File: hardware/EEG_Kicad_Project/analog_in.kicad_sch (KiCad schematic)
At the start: 1 part, among them U3 ADS1299

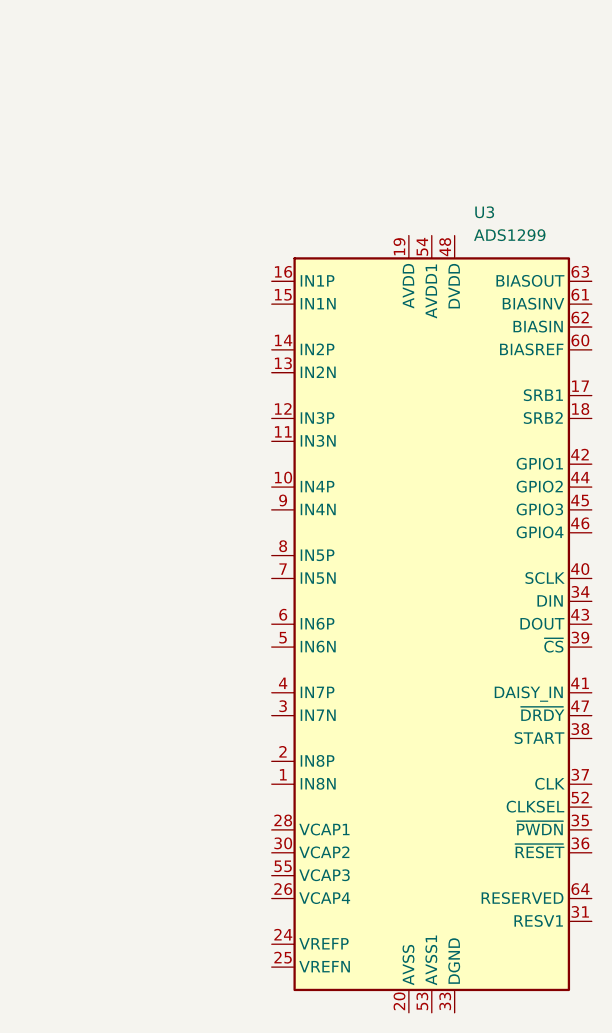
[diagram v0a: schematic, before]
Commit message: Add USB galvanic isolation barrier for patient safety
Adds a USB-C receptacle -> ESD protection -> ADuM3160 isolator ->
isolated TMU3-0511 DC-DC chain, separating the STM32/ADS1299/analog
supply (now fully isolated) from the non-isolated USB-connector side.
Closes the previously-floating USB_OTG_FS_DP/DM pins on the STM32,
adds CC1/CC2 pulldowns and VBUS decoupling on the new receptacle, and
fixes ADuM3160 VBUS2 tie per datasheet. Verified via kicad-happy: no
ERC regressions, isolation barrier confirmed intact (no net bridges
GND_PRI/+5V_PRI with the isolated GNDA/+5V/+3V3 domain).

Co-Authored-By: Claude Sonnet 5 <noreply@anthropic.com>
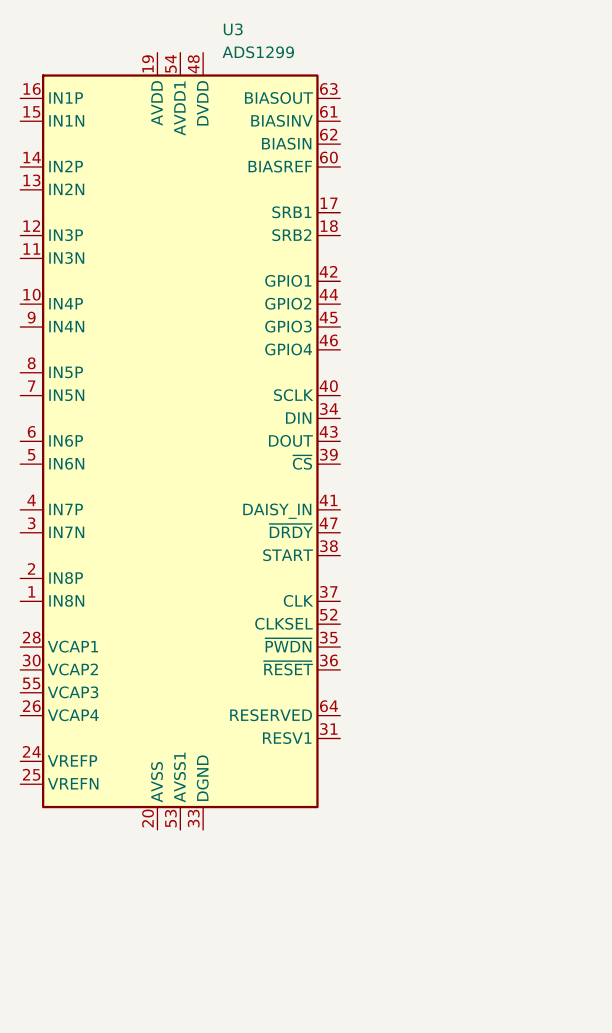
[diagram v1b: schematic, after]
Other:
- moved on the sheet: U3
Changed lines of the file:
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@@
 	(symbol
 		(lib_id "Analog_ADC:ADS1299")
-		(at 217.17 105.41 0)
+		(at 189.23 85.09 0)
 		(unit 1)
 		(exclude_from_sim no)
@@
 		(fields_autoplaced yes)
 		(property "Reference" "U3"
-			(at 221.8533 59.69 0)
+			(at 193.9133 39.37 0)
 			(effects
 				(font
@@
 		)
 		(property "Value" "ADS1299"
-			(at 221.8533 62.23 0)
+			(at 193.9133 41.91 0)
 			(effects
 				(font
@@
 		)
 		(property "Footprint" "Package_QFP:TQFP-64_10x10mm_P0.5mm"
-			(at 217.17 158.75 0)
+			(at 189.23 138.43 0)
 			(effects
 				(font
@@
 		)
 		(property "Datasheet" "https://www.ti.com/lit/ds/symlink/ads1299.pdf"
-			(at 217.17 161.29 0)
+			(at 189.23 140.97 0)
 			(effects
 				(font
@@
 		)
 		(property "Description" "Low-Noise, 8-channel, 24-bit ADC for EEG and Biopotential Measurements, TQFP-64"
-			(at 217.17 107.95 0)
+			(at 189.23 87.63 0)
 			(effects
 				(font
